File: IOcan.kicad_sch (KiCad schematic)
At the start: 0 parts

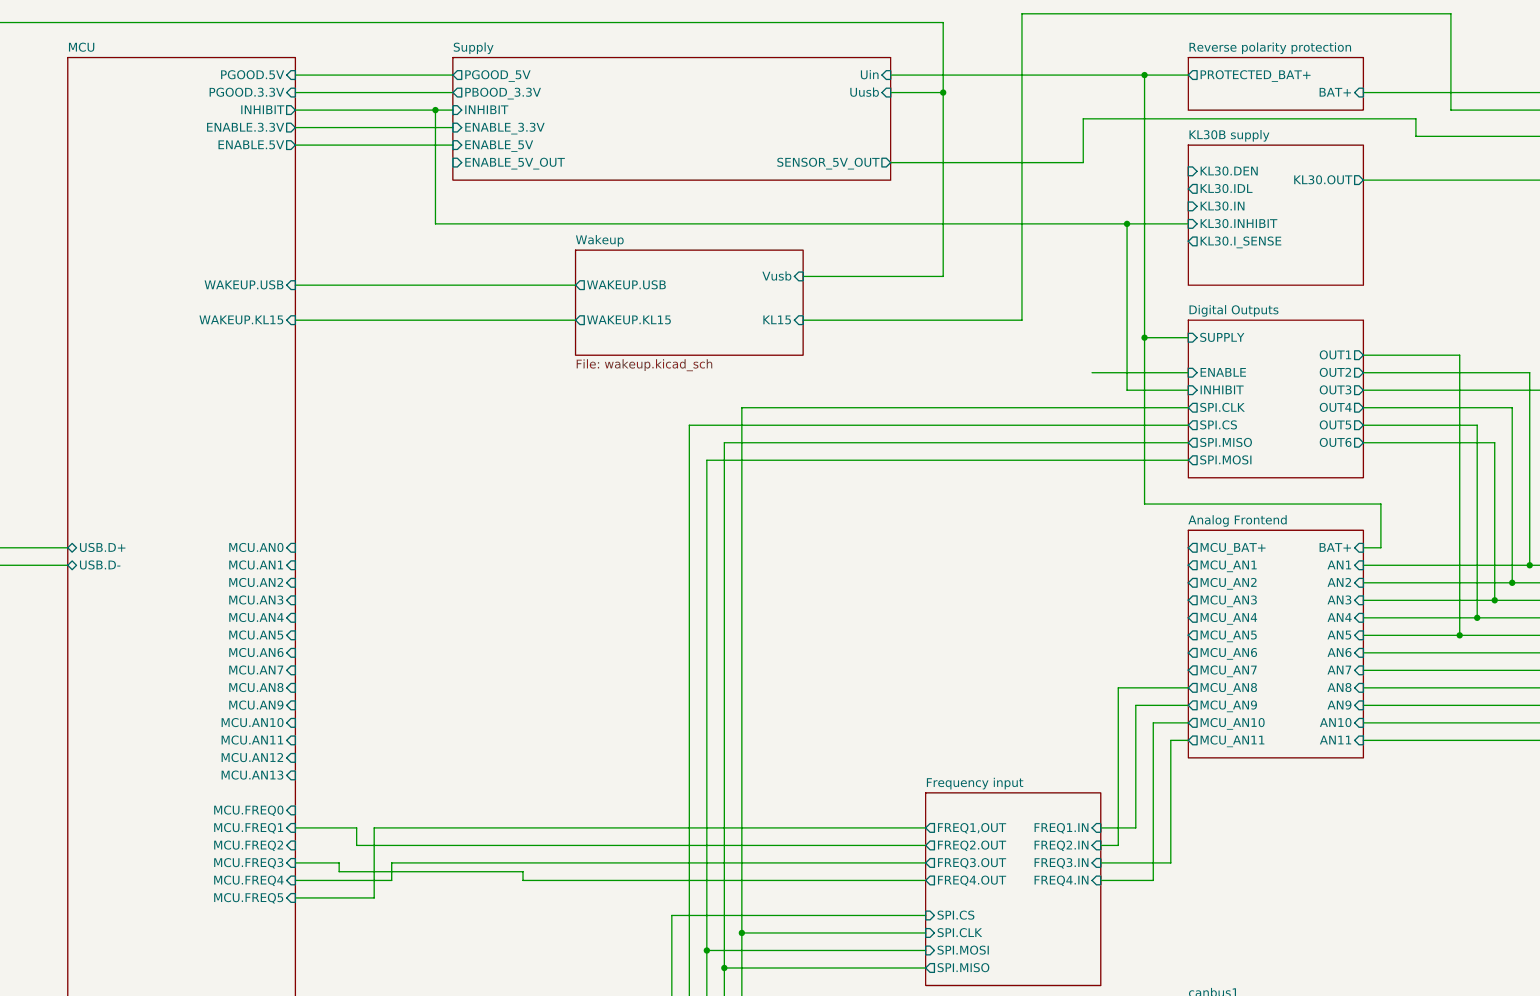
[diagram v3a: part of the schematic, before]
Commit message: Added missing parts of IOcan schematic
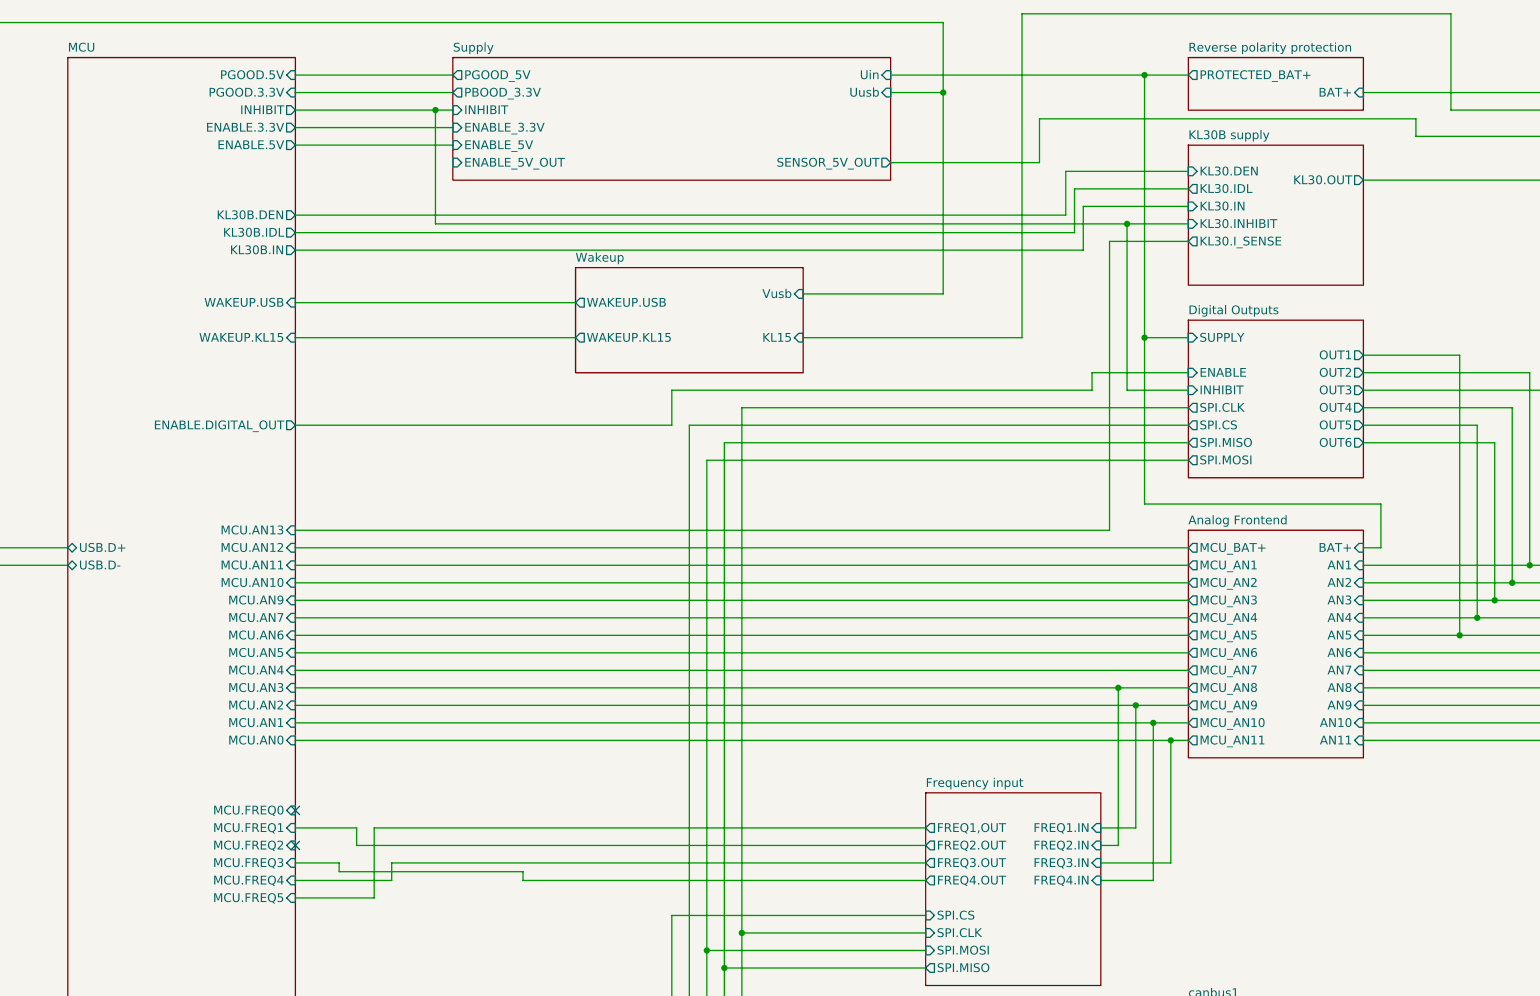
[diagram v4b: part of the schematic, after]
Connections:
- no-connect marks 0 -> 2
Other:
- sheet MCU ports: added ENABLE.DIGITAL_OUT, KL30B.DEN, KL30B.IDL, KL30B.IN; removed MCU.AN8

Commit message: Checked pinouts
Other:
- sheet MCU ports: added 5V_OUT_ENABLE; removed none
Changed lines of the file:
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@@
+	(wire
+		(pts
+			(xy 167.64 38.1) (xy 190.5 38.1)
+		)
+		(stroke
+			(width 0)
+			(type default)
+		)
+	)
 	(wire
 		(pts
@@
 			(effects
 				(font
+					(size 1.27 1.27)
+				)
+				(justify right)
+			)
+		)
+		(pin "5V_OUT_ENABLE" input
+			(at 167.64 38.1 0)
+			(effects
+				(font
